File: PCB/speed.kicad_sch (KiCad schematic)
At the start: 19 parts, among them U501 LMV321

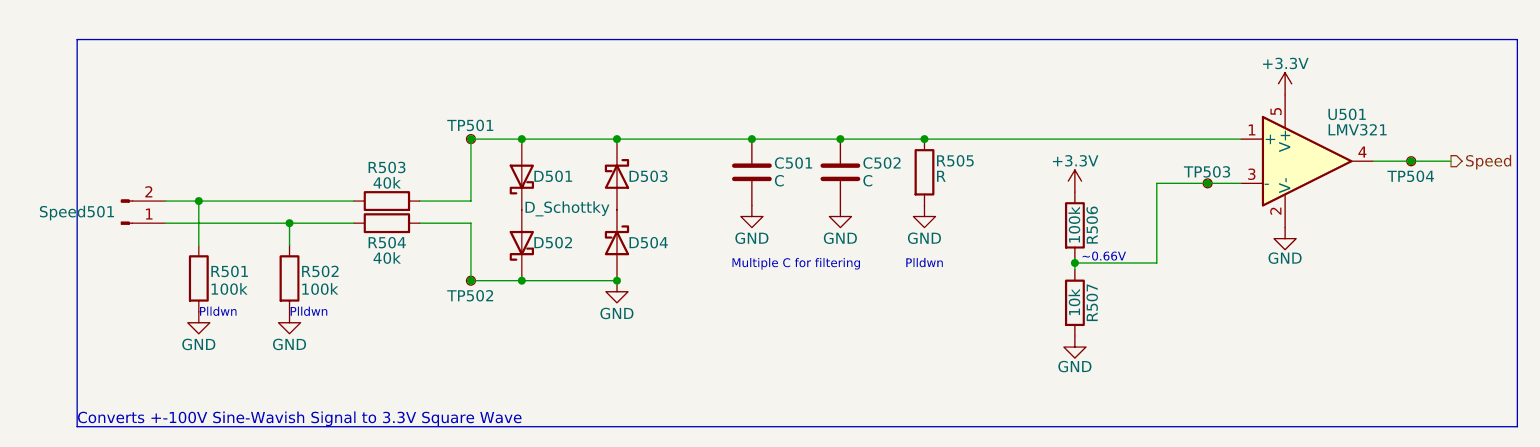
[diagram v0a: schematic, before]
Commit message: Applied recommendations from my coworker; Fixed badly placed filter caps; Added flyback diode to fan circuit; Applied larger grid and some spacing to the schematics; And some other small adjustments
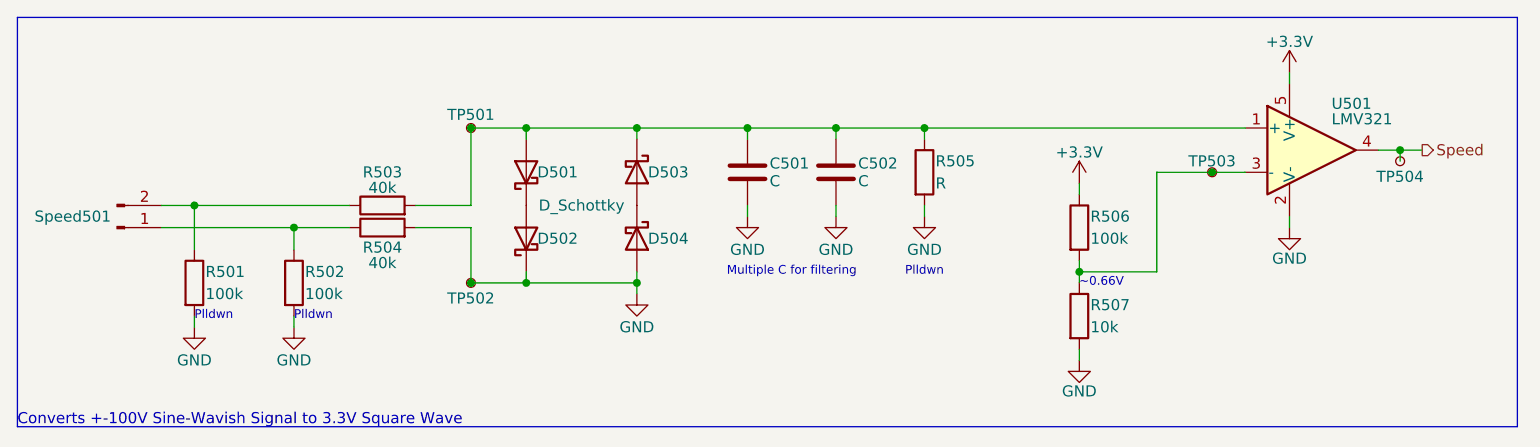
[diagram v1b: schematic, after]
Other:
- title: (none) -> Speed
- moved on the sheet: C501, C502, D501, D502, D503, D504, R501, R502, R503, R504, R506, R507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

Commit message: Changed some resistor and capacitor values;Added additional input electrolytic cap;Selected LCSC parts;Added diode footprint;Removed 3.3V power supply and decreased the output of the 5V supply to 3.3V;Added flyback diode on the fan circuit;Added LDO between the USB-C VBUS and the 5V rail
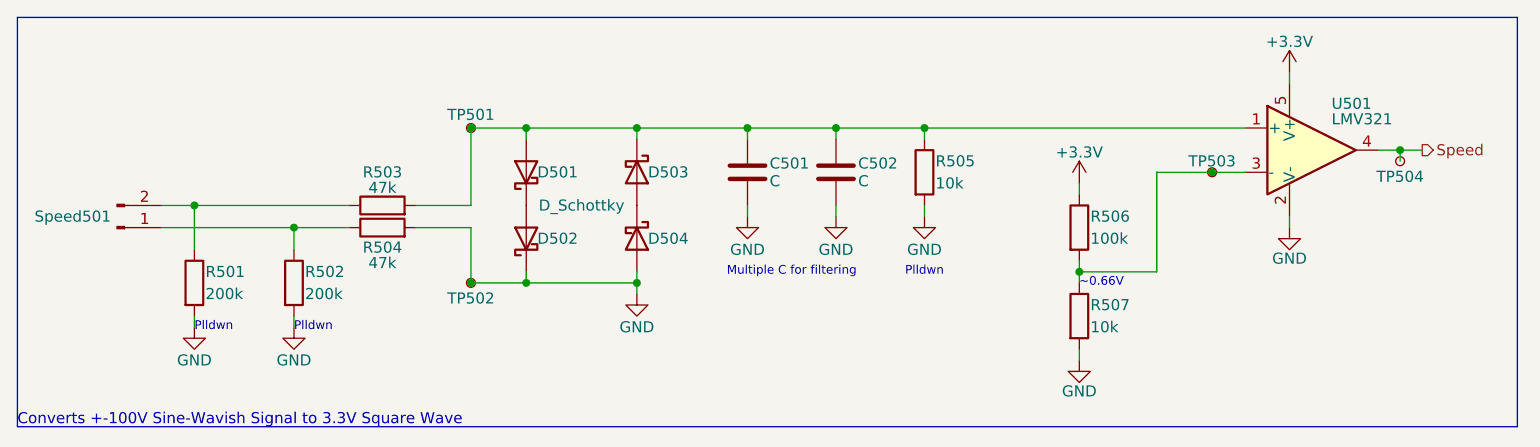
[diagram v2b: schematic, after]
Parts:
- D501, D502, D503, D504: footprint Diode_SMD:D_0805_2012Metric -> customFootprints:SOD-323HE
- R501, R502: value 100k -> 200k
- R503, R504: value 40k -> 47k
- R505: value R -> 10k; footprint Resistor_SMD:R_0805_2012Metric -> Resistor_SMD:R_0603_1608Metric; now in the parts list
- R506, R507: footprint Resistor_SMD:R_0805_2012Metric -> Resistor_SMD:R_0603_1608Metric
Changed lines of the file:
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@@
 	(text "Plldwn"
 		(exclude_from_sim no)
-		(at 106.68 102.87 0)
+		(at 106.68 104.14 0)
 		(effects
 			(font
@@
 	(text "Plldwn"
 		(exclude_from_sim no)
-		(at 95.25 102.87 0)
+		(at 95.25 104.14 0)
 		(effects
 			(font
@@
 		(unit 1)
 		(exclude_from_sim yes)
-		(in_bom no)
+		(in_bom yes)
 		(on_board yes)
 		(dnp no)
@@
 			)
 		)
-		(property "Value" "R"
+		(property "Value" "10k"
 			(at 180.34 87.63 0)
 			(effects
@@
 			)
 		)
-		(property "Footprint" "Resistor_SMD:R_0805_2012Metric"
+		(property "Footprint" "Resistor_SMD:R_0603_1608Metric"
 			(at 177.292 86.36 90)
 			(effects
@@
 			)
 		)
-		(property "Footprint" "Diode_SMD:D_0805_2012Metric"
+		(property "Footprint" "customFootprints:SOD-323HE"
 			(at 146.05 93.98 0)
 			(effects
@@
 			)
 		)
-		(property "Footprint" "Diode_SMD:D_0805_2012Metric"
+		(property "Footprint" "customFootprints:SOD-323HE"
 			(at 146.05 86.36 0)
 			(effects
@@
 			)
 		)
-		(property "Value" "40k"
+		(property "Value" "47k"
 			(at 116.84 88.138 90)
 			(effects
@@
 			)
 		)
-		(property "Value" "100k"
+		(property "Value" "200k"
 			(at 96.52 100.33 0)
 			(effects
@@
 			)
 		)
-		(property "Footprint" "Diode_SMD:D_0805_2012Metric"
+		(property "Footprint" "customFootprints:SOD-323HE"
 			(at 133.35 86.36 0)
 			(effects
@@
 			)
 		)
-		(property "Value" "100k"
+		(property "Value" "200k"
 			(at 107.95 100.33 0)
 			(effects
@@
 			)
 		)
-		(property "Value" "40k"
+		(property "Value" "47k"
 			(at 116.84 96.774 90)
 			(effects
@@
 			)
 		)
-		(property "Footprint" "Resistor_SMD:R_0805_2012Metric"
+		(property "Footprint" "Resistor_SMD:R_0603_1608Metric"
 			(at 195.072 92.71 90)
 			(effects
@@
 			)
 		)
-		(property "Footprint" "Diode_SMD:D_0805_2012Metric"
+		(property "Footprint" "customFootprints:SOD-323HE"
 			(at 133.35 93.98 0)
 			(effects
@@
 			)
 		)
-		(property "Footprint" "Resistor_SMD:R_0805_2012Metric"
+		(property "Footprint" "Resistor_SMD:R_0603_1608Metric"
 			(at 195.072 102.87 90)
 			(effects
